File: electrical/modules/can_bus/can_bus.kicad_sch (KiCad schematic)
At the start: 12 parts, among them U601 TCAN330DR

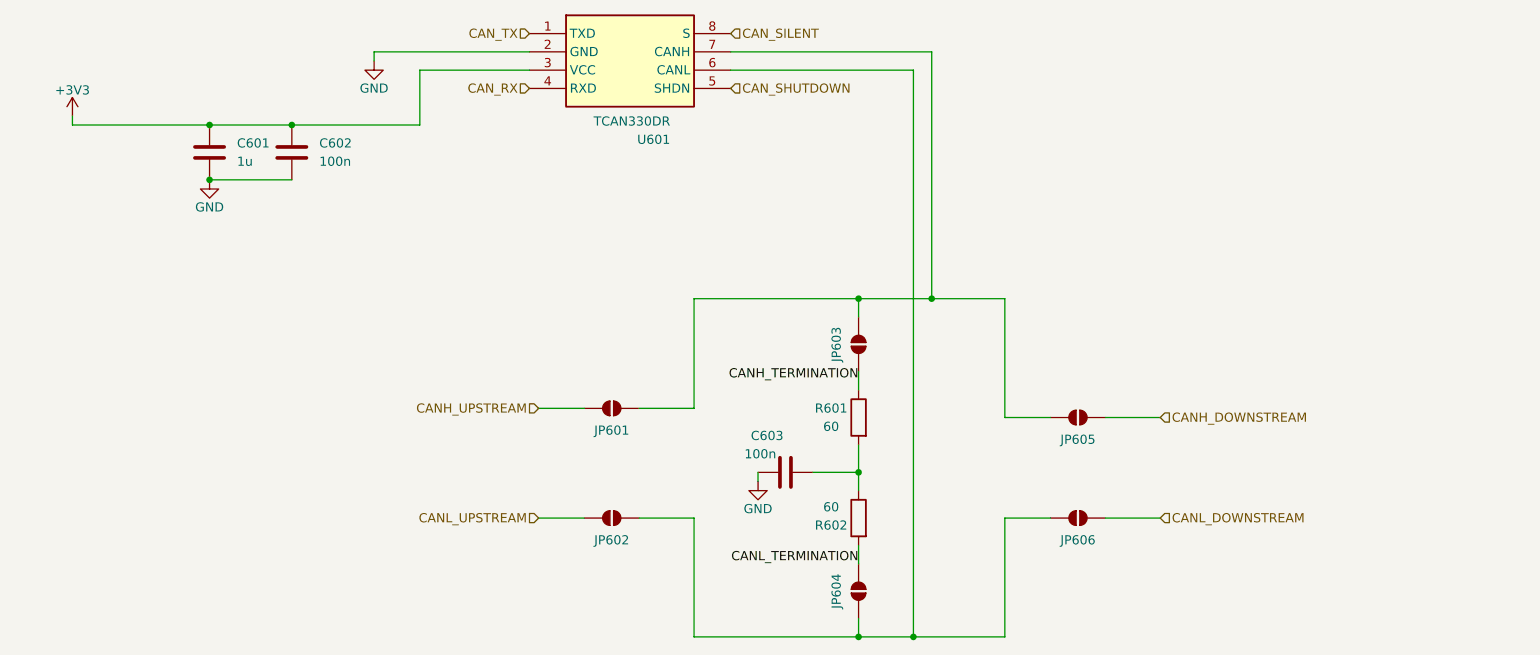
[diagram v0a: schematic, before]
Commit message: Move CAN bus to module. Layout circuitry for the CAN bus.
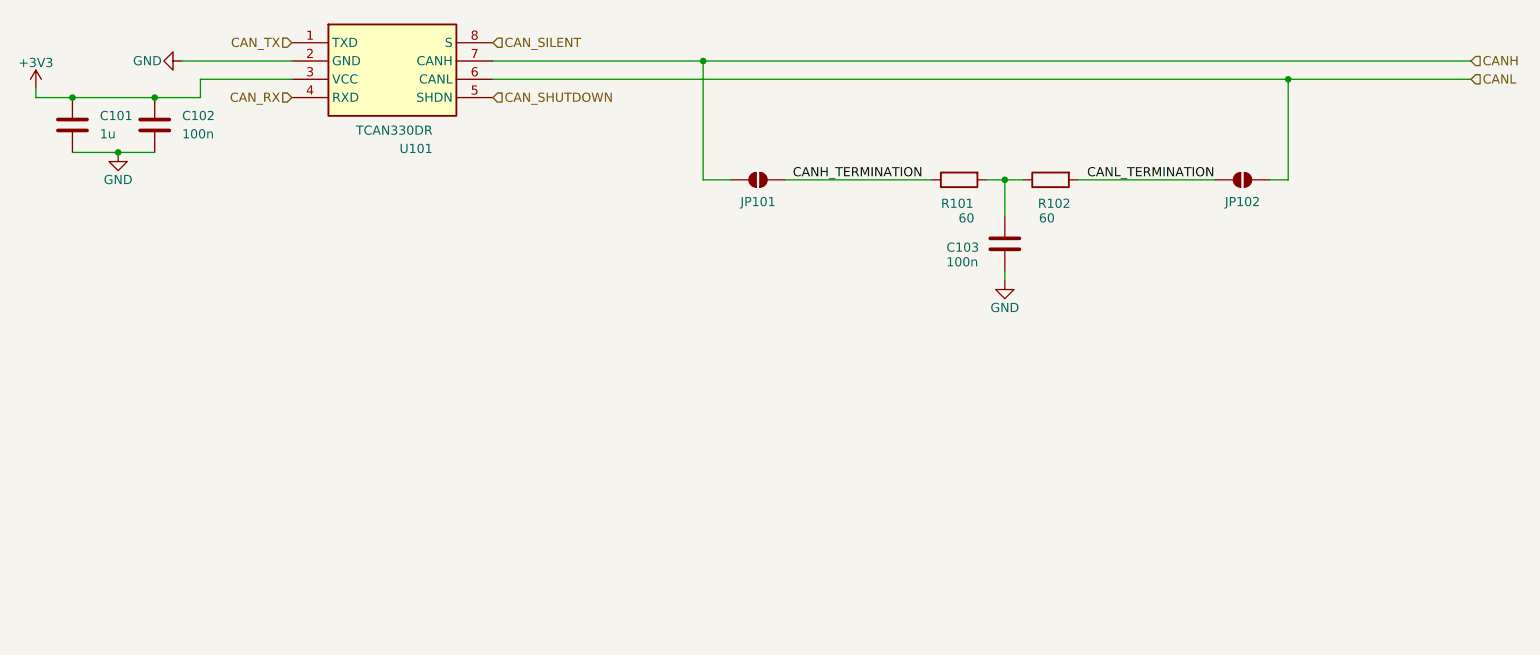
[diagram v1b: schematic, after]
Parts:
- removed JP601, JP602, JP605, JP606: SolderJumper_2_Open, Jumper:SolderJumper-2_P1.3mm_Open_RoundedPad1.0x1.5mm, symbol Jumper:SolderJumper_2_Open
- renumbered C601 to C101, C602 to C102, C603 to C103, JP603 to JP101, JP604 to JP102, R601 to R101, R602 to R102, U601 to U101
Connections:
- net CANH: now reaches JP101.1 (A), U101.7 (CANH)
- net CANL: now reaches JP102.2 (B), U101.6 (CANL)
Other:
- company: TVSC -> (none)
- title: 1s3p Battery Board -> CAN bus module
- moved on the sheet: C101, C102, C103, JP101, JP102, R101, R102, U101

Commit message: Attempt to find a pattern to unify component designators. It looks like the best workflow will be to re-annotate the schematic of each module, sync the PCB to the schematic without relinking based on the designators, and then letting the board project use the designators directly, without re-annotating at that level. Need to investigate the effect of this workflow on the BOM and gerber files.
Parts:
- renumbered C101 to C601, C102 to C602, C103 to C603, JP101 to JP601, JP102 to JP602, R101 to R601, R102 to R602, U101 to U601
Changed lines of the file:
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@@
 		(on_board yes)
 		(dnp no)
-		(property "Reference" "C103"
+		(property "Reference" "C603"
 			(at 173.228 77.978 0)
 			(effects
@@
 			(project "1s3p_battery_board"
 				(path "/695f882b-5312-4493-b26d-8f7d6768a9db/d470ef27-6c0f-4ffa-83b6-2c4b3c9c5ff3"
-					(reference "C?")
+					(reference "C603")
 					(unit 1)
 				)
@@
 		(on_board yes)
 		(dnp no)
-		(property "Reference" "U101"
+		(property "Reference" "U601"
 			(at 99.568 64.262 0)
 			(effects
@@
 			(project "1s3p_battery_board"
 				(path "/695f882b-5312-4493-b26d-8f7d6768a9db/d470ef27-6c0f-4ffa-83b6-2c4b3c9c5ff3"
-					(reference "U?")
+					(reference "U601")
 					(unit 1)
 				)
@@
 		(on_board yes)
 		(dnp no)
-		(property "Reference" "R102"
+		(property "Reference" "R602"
 			(at 185.928 71.882 90)
 			(effects
@@
 			(project "1s3p_battery_board"
 				(path "/695f882b-5312-4493-b26d-8f7d6768a9db/d470ef27-6c0f-4ffa-83b6-2c4b3c9c5ff3"
-					(reference "R?")
+					(reference "R602")
 					(unit 1)
 				)
@@
 		(on_board yes)
 		(dnp no)
-		(property "Reference" "#PWR0103"
+		(property "Reference" "#PWR0603"
 			(at 58.42 52.07 0)
 			(effects
@@
 			(project "1s3p_battery_board"
 				(path "/695f882b-5312-4493-b26d-8f7d6768a9db/d470ef27-6c0f-4ffa-83b6-2c4b3c9c5ff3"
-					(reference "#PWR?")
+					(reference "#PWR0603")
 					(unit 1)
 				)
@@
 		(on_board yes)
 		(dnp no)
-		(property "Reference" "JP101"
+		(property "Reference" "JP601"
 			(at 144.78 72.39 0)
 			(effects
@@
 			(project "1s3p_battery_board"
 				(path "/695f882b-5312-4493-b26d-8f7d6768a9db/d470ef27-6c0f-4ffa-83b6-2c4b3c9c5ff3"
-					(reference "JP?")
+					(reference "JP601")
 					(unit 1)
 				)
@@
 		(on_board yes)
 		(dnp no)
-		(property "Reference" "#PWR0102"
+		(property "Reference" "#PWR0602"
 			(at 55.88 71.12 0)
 			(effects
@@
 			(project "1s3p_battery_board"
 				(path "/695f882b-5312-4493-b26d-8f7d6768a9db/d470ef27-6c0f-4ffa-83b6-2c4b3c9c5ff3"
-					(reference "#PWR?")
+					(reference "#PWR0602")
 					(unit 1)
 				)
@@
 		(on_board yes)
 		(dnp no)
-		(property "Reference" "#PWR0104"
+		(property "Reference" "#PWR0604"
 			(at 179.07 88.9 0)
 			(effects
@@
 			(project "1s3p_battery_board"
 				(path "/695f882b-5312-4493-b26d-8f7d6768a9db/d470ef27-6c0f-4ffa-83b6-2c4b3c9c5ff3"
-					(reference "#PWR?")
+					(reference "#PWR0604")
 					(unit 1)
 				)
@@
 		(on_board yes)
 		(dnp no)
-		(property "Reference" "JP102"
+		(property "Reference" "JP602"
 			(at 212.09 72.39 0)
 			(effects
@@
 			(project "1s3p_battery_board"
 				(path "/695f882b-5312-4493-b26d-8f7d6768a9db/d470ef27-6c0f-4ffa-83b6-2c4b3c9c5ff3"
-					(reference "JP?")
+					(reference "JP602")
 					(unit 1)
 				)
@@
 		(on_board yes)
 		(dnp no)
-		(property "Reference" "#PWR0101"
+		(property "Reference" "#PWR0601"
 			(at 44.45 59.69 0)
 			(effects
@@
 			(project "1s3p_battery_board"
 				(path "/695f882b-5312-4493-b26d-8f7d6768a9db/d470ef27-6c0f-4ffa-83b6-2c4b3c9c5ff3"
-					(reference "#PWR?")
+					(reference "#PWR0601")
 					(unit 1)
 				)
@@
 		(dnp no)
 		(fields_autoplaced yes)
-		(property "Reference" "C102"
+		(property "Reference" "C602"
 			(at 64.77 59.69 0)
 			(effects
@@
 			(project "1s3p_battery_board"
 				(path "/695f882b-5312-4493-b26d-8f7d6768a9db/d470ef27-6c0f-4ffa-83b6-2c4b3c9c5ff3"
-					(reference "C?")
+					(reference "C602")
 					(unit 1)
 				)
@@
 		(on_board yes)
 		(dnp no)
-		(property "Reference" "R101"
+		(property "Reference" "R601"
 			(at 172.466 71.882 90)
 			(effects
@@
 			(project "1s3p_battery_board"
 				(path "/695f882b-5312-4493-b26d-8f7d6768a9db/d470ef27-6c0f-4ffa-83b6-2c4b3c9c5ff3"
-					(reference "R?")
+					(reference "R601")
 					(unit 1)
 				)
@@
 		(dnp no)
 		(fields_autoplaced yes)
-		(property "Reference" "C101"
+		(property "Reference" "C601"
 			(at 53.34 59.69 0)
 			(effects
@@
 			(project "1s3p_battery_board"
 				(path "/695f882b-5312-4493-b26d-8f7d6768a9db/d470ef27-6c0f-4ffa-83b6-2c4b3c9c5ff3"
-					(reference "C?")
-					(unit 1)
-				)
+					(reference "C601")
+					(unit 1)
+				)

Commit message: Update directionality of hierarchical labels and sheet pins.
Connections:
- net +3V3 renamed 3V3
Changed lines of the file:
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@@
+	(wire
+		(pts
+			(xy 44.45 52.07) (xy 45.72 52.07)
+		)
+		(stroke
+			(width 0)
+			(type default)
+		)
+	)
 	(wire
 		(pts
@@
 	(wire
 		(pts
+			(xy 44.45 52.07) (xy 44.45 57.15)
+		)
+		(stroke
+			(width 0)
+			(type default)
+		)
+	)
+	(wire
+		(pts
 			(xy 60.96 57.15) (xy 67.31 57.15)
 		)
@@
 		(pts
 			(xy 140.97 68.58) (xy 137.16 68.58)
-		)
-		(stroke
-			(width 0)
-			(type default)
-		)
-	)
-	(wire
-		(pts
-			(xy 44.45 55.88) (xy 44.45 57.15)
 		)
 		(stroke
@@
 	)
 	(hierarchical_label "CAN_TX"
-		(shape input)
+		(shape bidirectional)
 		(at 80.01 49.53 180)
 		(effects
@@
 	)
 	(hierarchical_label "CAN_RX"
-		(shape input)
+		(shape bidirectional)
 		(at 80.01 57.15 180)
 		(effects
@@
 	)
 	(hierarchical_label "CANL"
+		(shape bidirectional)
+		(at 243.84 54.61 0)
+		(effects
+			(font
+				(size 1.27 1.27)
+			)
+			(justify left)
+		)
+	)
+	(hierarchical_label "3V3"
 		(shape input)
-		(at 243.84 54.61 0)
+		(at 45.72 52.07 0)
 		(effects
 			(font
@@
 	)
 	(hierarchical_label "CANH"
-		(shape input)
+		(shape bidirectional)
 		(at 243.84 52.07 0)
 		(effects
@@
 					(unit 1)
 				)
-			)
-		)
-	)
-	(symbol
-		(lib_id "power:+3V3")
-		(at 44.45 55.88 0)
-		(unit 1)
-		(exclude_from_sim no)
-		(in_bom yes)
-		(on_board yes)
-		(dnp no)
-		(property "Reference" "#PWR0601"
-			(at 44.45 59.69 0)
-			(effects
-				(font
-					(size 1.27 1.27)
-				)
-				(hide yes)
-			)
-		)
-		(property "Value" "+3V3"
-			(at 44.45 52.324 0)
-			(effects
-				(font
-					(size 1.27 1.27)
-				)
-			)
-		)
-		(property "Footprint" ""
-			(at 44.45 55.88 0)
-			(effects
-				(font
-					(size 1.27 1.27)
-				)
-				(hide yes)
-			)
-		)
-		(property "Datasheet" ""
-			(at 44.45 55.88 0)
-			(effects
-				(font
-					(size 1.27 1.27)
-				)
-				(hide yes)
-			)
-		)
-		(property "Description" "Power symbol creates a global label with name \"+3V3\""
-			(at 44.45 55.88 0)
-			(effects
-				(font
-					(size 1.27 1.27)
-				)
-				(hide yes)
-			)
-		)
-		(pin "1"
-		)
-		(instances
-			(project "1s3p_battery_board"
-				(path "/695f882b-5312-4493-b26d-8f7d6768a9db/d470ef27-6c0f-4ffa-83b6-2c4b3c9c5ff3"
-					(reference "#PWR0601")
-					(unit 1)
-				)
-			)
-			(project "can_bus"
-				(path "/92465487-256a-4cb1-9bd2-6d40463e6535"
-					(reference "#PWR0101")
-					(unit 1)
-				)

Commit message: Update CAN bus module and connect it.
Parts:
- renumbered C601 to C101, C602 to C102, C603 to C103, JP601 to JP101, JP602 to JP102, R601 to R101, R602 to R102, U601 to U101
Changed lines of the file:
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@@
 		(on_board yes)
 		(dnp no)
-		(property "Reference" "C603"
+		(property "Reference" "C103"
 			(at 173.228 77.978 0)
 			(effects
@@
 		(on_board yes)
 		(dnp no)
-		(property "Reference" "U601"
+		(property "Reference" "U101"
 			(at 99.568 64.262 0)
 			(effects
@@
 		(on_board yes)
 		(dnp no)
-		(property "Reference" "R602"
+		(property "Reference" "R102"
 			(at 185.928 71.882 90)
 			(effects
@@
 		(on_board yes)
 		(dnp no)
-		(property "Reference" "#PWR0603"
+		(property "Reference" "#PWR0102"
 			(at 58.42 52.07 0)
 			(effects
@@
 			(project "can_bus"
 				(path "/92465487-256a-4cb1-9bd2-6d40463e6535"
-					(reference "#PWR0103")
+					(reference "#PWR0102")
 					(unit 1)
 				)
@@
 		(on_board yes)
 		(dnp no)
-		(property "Reference" "JP601"
+		(property "Reference" "JP101"
 			(at 144.78 72.39 0)
 			(effects
@@
 		(on_board yes)
 		(dnp no)
-		(property "Reference" "#PWR0602"
+		(property "Reference" "#PWR0101"
 			(at 55.88 71.12 0)
 			(effects
@@
 			(project "can_bus"
 				(path "/92465487-256a-4cb1-9bd2-6d40463e6535"
-					(reference "#PWR0102")
+					(reference "#PWR0101")
 					(unit 1)
 				)
@@
 		(on_board yes)
 		(dnp no)
-		(property "Reference" "#PWR0604"
+		(property "Reference" "#PWR0103"
 			(at 179.07 88.9 0)
 			(effects
@@
 			(project "can_bus"
 				(path "/92465487-256a-4cb1-9bd2-6d40463e6535"
-					(reference "#PWR0104")
+					(reference "#PWR0103")
 					(unit 1)
 				)
@@
 		(on_board yes)
 		(dnp no)
-		(property "Reference" "JP602"
+		(property "Reference" "JP102"
 			(at 212.09 72.39 0)
 			(effects
@@
 		(dnp no)
 		(fields_autoplaced yes)
-		(property "Reference" "C602"
+		(property "Reference" "C102"
 			(at 64.77 59.69 0)
 			(effects
@@
 		(on_board yes)
 		(dnp no)
-		(property "Reference" "R601"
+		(property "Reference" "R101"
 			(at 172.466 71.882 90)
 			(effects
@@
 		(dnp no)
 		(fields_autoplaced yes)
-		(property "Reference" "C601"
+		(property "Reference" "C101"
 			(at 53.34 59.69 0)
 			(effects

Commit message: Complete fanout of CAN bus controller and related passive components.
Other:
- company: (none) -> TVSC
- title: CAN bus module -> ${PCB_NAME}
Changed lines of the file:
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@@
 	(paper "USLetter")
 	(title_block
-		(title "CAN bus module")
-		(date "2026-07-28")
+		(title "${PCB_NAME}")
+		(date "2026-07-11")
+		(rev "${PCB_VERSION}")
+		(company "TVSC")
 	)
 	(junction
@@
 			)
 		)
+		(property "Purpose" ""
+			(at 179.07 77.47 0)
+			(effects
+				(font
+					(size 1.27 1.27)
+				)
+				(hide yes)
+			)
+		)
 		(pin "1"
 		)
@@
 		(instances
 			(project "1s3p_battery_board"
-				(path "/695f882b-5312-4493-b26d-8f7d6768a9db/d470ef27-6c0f-4ffa-83b6-2c4b3c9c5ff3"
-					(reference "C603")
+				(path "/695f882b-5312-4493-b26d-8f7d6768a9db/e0e5088b-2fa2-4f34-adc6-d0f708744404/d470ef27-6c0f-4ffa-83b6-2c4b3c9c5ff3"
+					(reference "C503")
 					(unit 1)
 				)
@@
 			)
 		)
+		(property "Purpose" ""
+			(at 80.01 49.53 0)
+			(effects
+				(font
+					(size 1.27 1.27)
+				)
+				(hide yes)
+			)
+		)
 		(pin "2"
 		)
@@
 		(instances
 			(project "1s3p_battery_board"
-				(path "/695f882b-5312-4493-b26d-8f7d6768a9db/d470ef27-6c0f-4ffa-83b6-2c4b3c9c5ff3"
-					(reference "U601")
+				(path "/695f882b-5312-4493-b26d-8f7d6768a9db/e0e5088b-2fa2-4f34-adc6-d0f708744404/d470ef27-6c0f-4ffa-83b6-2c4b3c9c5ff3"
+					(reference "U501")
 					(unit 1)
 				)
@@
 			)
 		)
+		(property "Purpose" ""
+			(at 185.42 68.58 90)
+			(effects
+				(font
+					(size 1.27 1.27)
+				)
+				(hide yes)
+			)
+		)
 		(pin "2"
 		)
@@
 		(instances
 			(project "1s3p_battery_board"
-				(path "/695f882b-5312-4493-b26d-8f7d6768a9db/d470ef27-6c0f-4ffa-83b6-2c4b3c9c5ff3"
-					(reference "R602")
+				(path "/695f882b-5312-4493-b26d-8f7d6768a9db/e0e5088b-2fa2-4f34-adc6-d0f708744404/d470ef27-6c0f-4ffa-83b6-2c4b3c9c5ff3"
+					(reference "R502")
 					(unit 1)
 				)
@@
 		(instances
 			(project "1s3p_battery_board"
-				(path "/695f882b-5312-4493-b26d-8f7d6768a9db/d470ef27-6c0f-4ffa-83b6-2c4b3c9c5ff3"
-					(reference "#PWR0603")
+				(path "/695f882b-5312-4493-b26d-8f7d6768a9db/e0e5088b-2fa2-4f34-adc6-d0f708744404/d470ef27-6c0f-4ffa-83b6-2c4b3c9c5ff3"
+					(reference "#PWR0502")
 					(unit 1)
 				)
@@
 			)
 		)
+		(property "Purpose" ""
+			(at 144.78 68.58 0)
+			(effects
+				(font
+					(size 1.27 1.27)
+				)
+				(hide yes)
+			)
+		)
 		(pin "2"
 		)
@@
 		(instances
 			(project "1s3p_battery_board"
-				(path "/695f882b-5312-4493-b26d-8f7d6768a9db/d470ef27-6c0f-4ffa-83b6-2c4b3c9c5ff3"
-					(reference "JP601")
+				(path "/695f882b-5312-4493-b26d-8f7d6768a9db/e0e5088b-2fa2-4f34-adc6-d0f708744404/d470ef27-6c0f-4ffa-83b6-2c4b3c9c5ff3"
+					(reference "JP501")
 					(unit 1)
 				)
@@
 		(instances
 			(project "1s3p_battery_board"
-				(path "/695f882b-5312-4493-b26d-8f7d6768a9db/d470ef27-6c0f-4ffa-83b6-2c4b3c9c5ff3"
-					(reference "#PWR0602")
+				(path "/695f882b-5312-4493-b26d-8f7d6768a9db/e0e5088b-2fa2-4f34-adc6-d0f708744404/d470ef27-6c0f-4ffa-83b6-2c4b3c9c5ff3"
+					(reference "#PWR0501")
 					(unit 1)
 				)
@@
 		(instances
 			(project "1s3p_battery_board"
-				(path "/695f882b-5312-4493-b26d-8f7d6768a9db/d470ef27-6c0f-4ffa-83b6-2c4b3c9c5ff3"
-					(reference "#PWR0604")
+				(path "/695f882b-5312-4493-b26d-8f7d6768a9db/e0e5088b-2fa2-4f34-adc6-d0f708744404/d470ef27-6c0f-4ffa-83b6-2c4b3c9c5ff3"
+					(reference "#PWR0503")
 					(unit 1)
 				)
@@
 			)
 		)
+		(property "Purpose" ""
+			(at 212.09 68.58 0)
+			(effects
+				(font
+					(size 1.27 1.27)
+				)
+				(hide yes)
+			)
+		)
 		(pin "2"
 		)
@@
 		(instances
 			(project "1s3p_battery_board"
-				(path "/695f882b-5312-4493-b26d-8f7d6768a9db/d470ef27-6c0f-4ffa-83b6-2c4b3c9c5ff3"
-					(reference "JP602")
+				(path "/695f882b-5312-4493-b26d-8f7d6768a9db/e0e5088b-2fa2-4f34-adc6-d0f708744404/d470ef27-6c0f-4ffa-83b6-2c4b3c9c5ff3"
+					(reference "JP502")
 					(unit 1)
 				)
@@
 			)
 		)
+		(property "Purpose" ""
+			(at 60.96 60.96 0)
+			(effects
+				(font
+					(size 1.27 1.27)
+				)
+				(hide yes)
+			)
+		)
 		(pin "1"
 		)
@@
 		(instances
 			(project "1s3p_battery_board"
-				(path "/695f882b-5312-4493-b26d-8f7d6768a9db/d470ef27-6c0f-4ffa-83b6-2c4b3c9c5ff3"
-					(reference "C602")
+				(path "/695f882b-5312-4493-b26d-8f7d6768a9db/e0e5088b-2fa2-4f34-adc6-d0f708744404/d470ef27-6c0f-4ffa-83b6-2c4b3c9c5ff3"
+					(reference "C502")
 					(unit 1)
 				)
@@
 			)
 		)
+		(property "Purpose" ""
+			(at 172.72 68.58 90)
+			(effects
+				(font
+					(size 1.27 1.27)
+				)
+				(hide yes)
+			)
+		)
 		(pin "2"
 		)
@@
 		(instances
 			(project "1s3p_battery_board"
-				(path "/695f882b-5312-4493-b26d-8f7d6768a9db/d470ef27-6c0f-4ffa-83b6-2c4b3c9c5ff3"
-					(reference "R601")
+				(path "/695f882b-5312-4493-b26d-8f7d6768a9db/e0e5088b-2fa2-4f34-adc6-d0f708744404/d470ef27-6c0f-4ffa-83b6-2c4b3c9c5ff3"
+					(reference "R501")
 					(unit 1)
 				)
@@
 			)
 		)
+		(property "Purpose" ""
+			(at 49.53 60.96 0)
+			(effects
+				(font
+					(size 1.27 1.27)
+				)
+				(hide yes)
+			)
+		)
 		(pin "1"
 		)
@@
 		(instances
 			(project "1s3p_battery_board"
-				(path "/695f882b-5312-4493-b26d-8f7d6768a9db/d470ef27-6c0f-4ffa-83b6-2c4b3c9c5ff3"
-					(reference "C601")
-					(unit 1)
-				)
+				(path "/695f882b-5312-4493-b26d-8f7d6768a9db/e0e5088b-2fa2-4f34-adc6-d0f708744404/d470ef27-6c0f-4ffa-83b6-2c4b3c9c5ff3"
+					(reference "C501")
+					(unit 1)
+				)
